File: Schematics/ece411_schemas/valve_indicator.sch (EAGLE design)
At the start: 66 parts, among them IC1 STM32F042K6T6, T1 2N2222, T2 2N2222, T3 2N2222, T4 2N2222, U1 DIODES_INC._AZ34063UMTR-G1DIO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, U2 DIODES_INC._AZ34063UMTR-G1DIO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

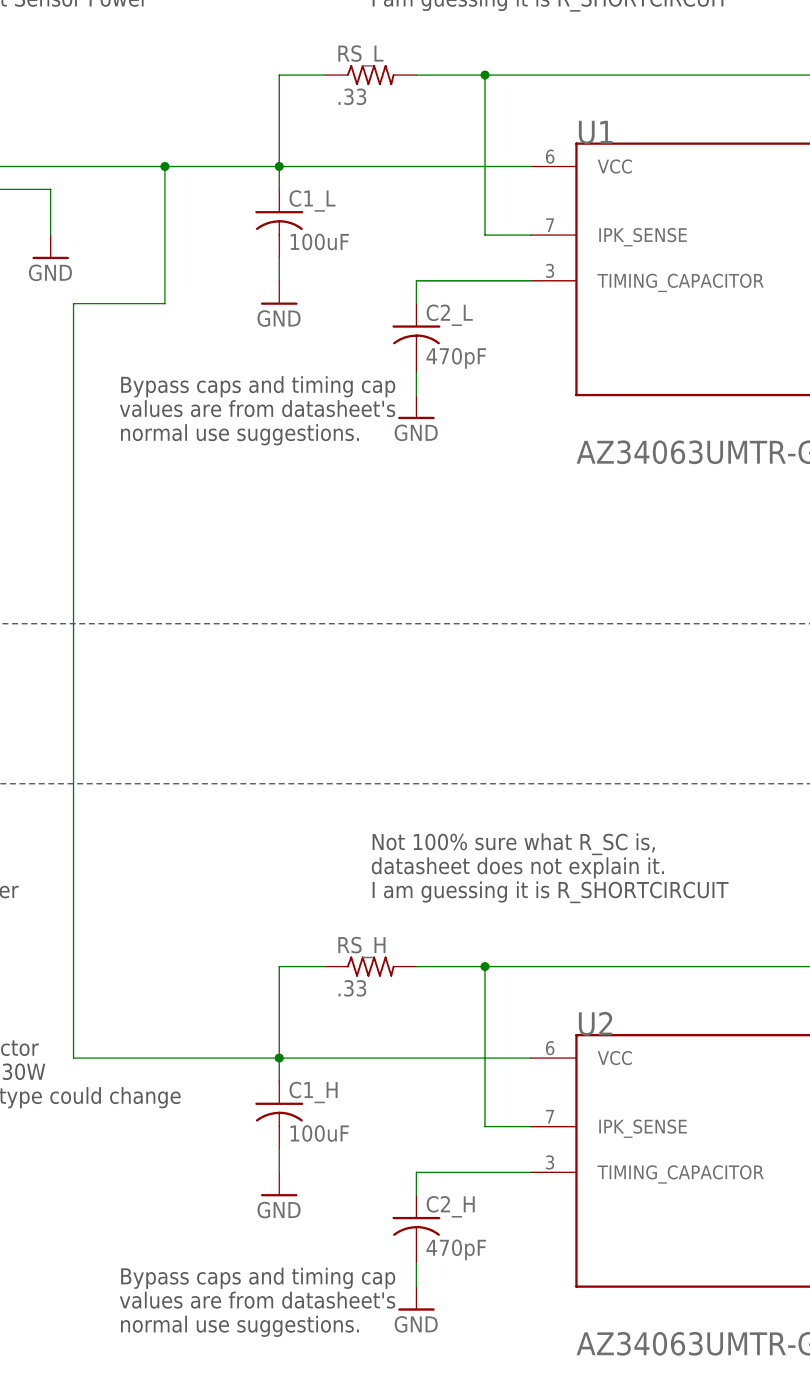
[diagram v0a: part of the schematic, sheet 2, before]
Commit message: added bypass caps, updated bom
needed to add 10uF ceramic in parallel with 100uF electro caps to decrease resistance to ground
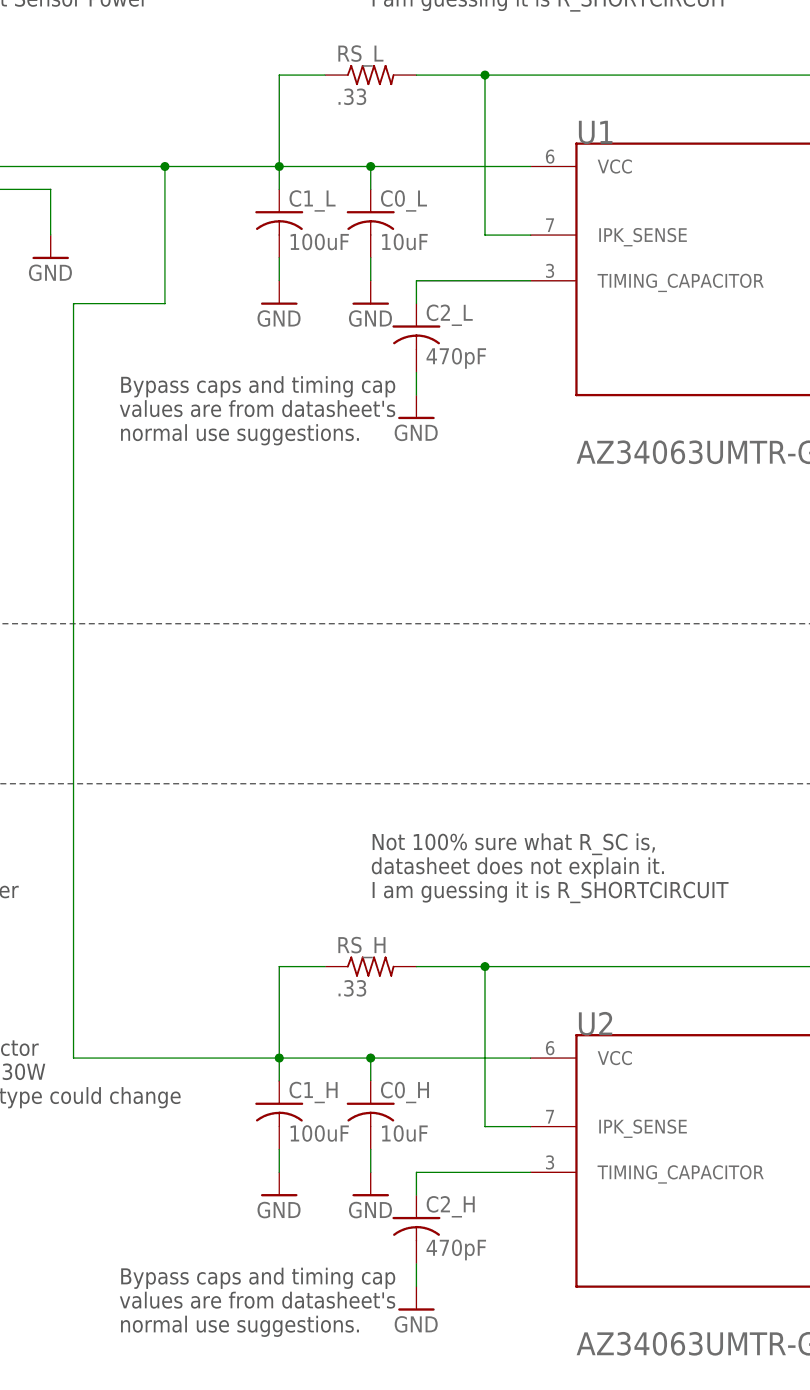
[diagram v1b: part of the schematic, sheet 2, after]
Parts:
- added C0_H, C0_L: 10uF, rcl:C-USC1206
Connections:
- net GND: now also C0_H.2, C0_L.2
- net N$1: now also C0_H.1, C0_L.1
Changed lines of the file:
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@@
 <attribute name="MPN" value="107CKR050M"/>
 </part>
+<part name="C0_L" library="rcl" library_urn="urn:adsk.eagle:library:334" deviceset="C-US" device="C1206" package3d_urn="urn:adsk.eagle:package:23618/2" value="10uF"/>
+<part name="C0_H" library="rcl" library_urn="urn:adsk.eagle:library:334" deviceset="C-US" device="C1206" package3d_urn="urn:adsk.eagle:package:23618/2" value="10uF"/>
+<part name="GND41" library="supply1" library_urn="urn:adsk.eagle:library:371" deviceset="GND" device=""/>
+<part name="GND42" library="supply1" library_urn="urn:adsk.eagle:library:371" deviceset="GND" device=""/>
 </parts>
 <sheets>
@@
 <attribute name="MFR" x="121.92" y="109.22" size="1.778" layer="96" display="off"/>
 </instance>
+<instance part="C0_L" gate="G$1" x="132.08" y="208.28" smashed="yes">
+<attribute name="NAME" x="133.096" y="208.915" size="1.778" layer="95"/>
+<attribute name="VALUE" x="133.096" y="204.089" size="1.778" layer="96"/>
+</instance>
+<instance part="C0_H" gate="G$1" x="132.08" y="109.22" smashed="yes">
+<attribute name="NAME" x="133.096" y="109.855" size="1.778" layer="95"/>
+<attribute name="VALUE" x="133.096" y="105.029" size="1.778" layer="96"/>
+</instance>
+<instance part="GND41" gate="1" x="132.08" y="99.06" smashed="yes">
+<attribute name="VALUE" x="129.54" y="96.52" size="1.778" layer="96"/>
+</instance>
+<instance part="GND42" gate="1" x="132.08" y="198.12" smashed="yes">
+<attribute name="VALUE" x="129.54" y="195.58" size="1.778" layer="96"/>
+</instance>
 </instances>
 <busses>
@@
 <wire x1="233.68" y1="228.6" x2="238.76" y2="228.6" width="0.1524" layer="91"/>
 <pinref part="R2_L" gate="G$1" pin="1"/>
+</segment>
+<segment>
+<pinref part="C0_H" gate="G$1" pin="2"/>
+<wire x1="132.08" y1="104.14" x2="132.08" y2="101.6" width="0.1524" layer="91"/>
+<pinref part="GND41" gate="1" pin="GND"/>
+</segment>
+<segment>
+<pinref part="GND42" gate="1" pin="GND"/>
+<pinref part="C0_L" gate="G$1" pin="2"/>
+<wire x1="132.08" y1="200.66" x2="132.08" y2="203.2" width="0.1524" layer="91"/>
 </segment>
 </net>
@@
 <segment>
 <pinref part="U2" gate="G$0" pin="VCC"/>
-<wire x1="121.92" y1="114.3" x2="149.86" y2="114.3" width="0.1524" layer="91"/>
+<wire x1="121.92" y1="114.3" x2="132.08" y2="114.3" width="0.1524" layer="91"/>
+<wire x1="132.08" y1="114.3" x2="149.86" y2="114.3" width="0.1524" layer="91"/>
 <wire x1="121.92" y1="111.76" x2="121.92" y2="114.3" width="0.1524" layer="91"/>
 <junction x="121.92" y="114.3"/>
@@
 <pinref part="U1" gate="G$0" pin="VCC"/>
 <wire x1="109.22" y1="213.36" x2="121.92" y2="213.36" width="0.1524" layer="91"/>
-<wire x1="121.92" y1="213.36" x2="149.86" y2="213.36" width="0.1524" layer="91"/>
+<wire x1="121.92" y1="213.36" x2="132.08" y2="213.36" width="0.1524" layer="91"/>
+<wire x1="132.08" y1="213.36" x2="149.86" y2="213.36" width="0.1524" layer="91"/>
 <wire x1="121.92" y1="210.82" x2="121.92" y2="213.36" width="0.1524" layer="91"/>
 <junction x="121.92" y="213.36"/>
@@
 <pinref part="C1_L" gate="G$1" pin="1"/>
 <pinref part="C1_H" gate="G$1" pin="1"/>
-</segment>
-</net>
+<pinref part="C0_H" gate="G$1" pin="1"/>
+<wire x1="132.08" y1="111.76" x2="132.08" y2="114.3" width="0.1524" layer="91"/>
+<junction x="132.08" y="114.3"/>
+<pinref part="C0_L" gate="G$1" pin="1"/>
+<wire x1="132.08" y1="210.82" x2="132.08" y2="213.36" width="0.1524" layer="91"/>
+<junction x="132.08" y="213.36"/>
+</segment>
+</net>

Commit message: added bat backup
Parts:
- added BATT_BACKUP: (no value), SparkFun-Connectors:JST_2MM_MALE
- added SB240: (no value), diode:SCHOTTKY-DIODECB417-15
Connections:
- new net N$10: SB240.C
- new net N$16: BATT_BACKUP.+, SB240.A
- net GND: now also BATT_BACKUP.-
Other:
- note added: "Battery Backup System:"
- note added: "Schottky Diode with 2A forward current. Safe to 40V reverse voltage. Forward voltage drop of 0.5v"
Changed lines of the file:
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@@
 <part name="GND41" library="supply1" library_urn="urn:adsk.eagle:library:371" deviceset="GND" device=""/>
 <part name="GND42" library="supply1" library_urn="urn:adsk.eagle:library:371" deviceset="GND" device=""/>
+<part name="BATT_BACKUP" library="SparkFun-Connectors" library_urn="urn:adsk.eagle:library:513" deviceset="JST_2MM_MALE" device="" package3d_urn="urn:adsk.eagle:package:38042/1"/>
+<part name="GND43" library="supply1" library_urn="urn:adsk.eagle:library:371" deviceset="GND" device=""/>
+<part name="SB240" library="diode" library_urn="urn:adsk.eagle:library:210" deviceset="SCHOTTKY-DIODE" device="CB417-15" package3d_urn="urn:adsk.eagle:package:43349/2"/>
 </parts>
 <sheets>
@@
 <text x="297.18" y="119.38" size="1.778" layer="97">10V power all LEDs and Buzzer</text>
 <text x="50.8" y="132.08" size="1.778" layer="97">POE+ Power Supply to 10V LED Power</text>
+<wire x1="340.36" y1="162.56" x2="48.26" y2="162.56" width="0.1524" layer="97" style="shortdash"/>
+<wire x1="48.26" y1="162.56" x2="48.26" y2="243.84" width="0.1524" layer="97" style="shortdash"/>
+<text x="12.7" y="182.88" size="1.778" layer="91">Battery Backup System:</text>
+<text x="33.02" y="165.1" size="1.778" layer="91">Schottky Diode with 2A forward current.
+Safe to 40V reverse voltage. Forward voltage drop of 0.5v</text>
 </plain>
 <instances>
@@
 <attribute name="VALUE" x="129.54" y="195.58" size="1.778" layer="96"/>
 </instance>
+<instance part="BATT_BACKUP" gate="G$1" x="15.24" y="172.72" smashed="yes">
+<attribute name="NAME" x="12.7" y="178.562" size="1.778" layer="95"/>
+</instance>
+<instance part="GND43" gate="1" x="15.24" y="154.94" smashed="yes">
+<attribute name="VALUE" x="12.7" y="152.4" size="1.778" layer="96"/>
+</instance>
+<instance part="SB240" gate="G$1" x="35.56" y="154.94" smashed="yes">
+<attribute name="NAME" x="33.274" y="156.845" size="1.778" layer="95"/>
+<attribute name="VALUE" x="33.274" y="151.511" size="1.778" layer="96"/>
+</instance>
 </instances>
 <busses>
@@
 <pinref part="C0_L" gate="G$1" pin="2"/>
 <wire x1="132.08" y1="200.66" x2="132.08" y2="203.2" width="0.1524" layer="91"/>
+</segment>
+<segment>
+<pinref part="BATT_BACKUP" gate="G$1" pin="-"/>
+<pinref part="GND43" gate="1" pin="GND"/>
+<wire x1="15.24" y1="167.64" x2="15.24" y2="157.48" width="0.1524" layer="91"/>
 </segment>
 </net>
@@
 </segment>
 </net>
+<net name="N$10" class="0">
+<segment>
+<pinref part="SB240" gate="G$1" pin="C"/>
+<wire x1="38.1" y1="154.94" x2="99.06" y2="154.94" width="0.1524" layer="91"/>
+</segment>
+</net>
+<net name="N$16" class="0">
+<segment>
+<pinref part="BATT_BACKUP" gate="G$1" pin="+"/>
+<pinref part="SB240" gate="G$1" pin="A"/>
+<wire x1="17.78" y1="167.64" x2="17.78" y2="154.94" width="0.1524" layer="91"/>
+<wire x1="17.78" y1="154.94" x2="33.02" y2="154.94" width="0.1524" layer="91"/>
+</segment>
+</net>

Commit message: updates to board, added libraries
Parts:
- removed JTAG_EMUL: JTAG_EMUL, pinhead:PINHD-1X5
- removed SB240: (no value), diode:SCHOTTKY-DIODECB417-15
- added D3: SB240, diode:1N5817-B
- added J1: 1.27MM-SWD-CONNECTOR, J-CNC-3220-10-0100-00-ARM-SWD-port:1.27MM-SWD-CONNECTOR
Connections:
- removed net N$10: SB240.C
- net GND: no longer JTAG_EMUL.2
- net N$1: now also D3.C
- net N$16: now also D3.A; no longer SB240.A
- net N$30: now also J1.SWDIO/TMS; no longer JTAG_EMUL.3
- net N$31: now also J1.SWDCLK/TCK; no longer JTAG_EMUL.4
- net N$9: no longer JTAG_EMUL.5
- net VCC: no longer JTAG_EMUL.1
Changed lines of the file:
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@@
 <part name="P+2" library="supply1" library_urn="urn:adsk.eagle:library:371" deviceset="VCC" device="" value="3V6"/>
 <part name="GND25" library="supply1" library_urn="urn:adsk.eagle:library:371" deviceset="GND" device=""/>
-<part name="JTAG_EMUL" library="pinhead" library_urn="urn:adsk.eagle:library:325" deviceset="PINHD-1X5" device="" package3d_urn="urn:adsk.eagle:package:22469/2" value="JTAG_EMUL"/>
 <part name="P+12" library="supply1" library_urn="urn:adsk.eagle:library:371" deviceset="VCC" device="" value="3V6"/>
 <part name="GND26" library="supply1" library_urn="urn:adsk.eagle:library:371" deviceset="GND" device=""/>
@@
 <part name="BATT_BACKUP" library="SparkFun-Connectors" library_urn="urn:adsk.eagle:library:513" deviceset="JST_2MM_MALE" device="" package3d_urn="urn:adsk.eagle:package:38042/1"/>
 <part name="GND43" library="supply1" library_urn="urn:adsk.eagle:library:371" deviceset="GND" device=""/>
-<part name="SB240" library="diode" library_urn="urn:adsk.eagle:library:210" deviceset="SCHOTTKY-DIODE" device="CB417-15" package3d_urn="urn:adsk.eagle:package:43349/2"/>
+<part name="D3" library="diode" library_urn="urn:adsk.eagle:library:210" deviceset="1N581*" device="" package3d_urn="urn:adsk.eagle:package:43421/1" technology="7-B" value="SB240"/>
+<part name="J1" library="J-CNC-3220-10-0100-00-ARM-SWD-port" deviceset="1.27MM-SWD-CONNECTOR" device=""/>
 </parts>
 <sheets>
@@
 <attribute name="VALUE" x="195.58" y="68.58" size="1.778" layer="96"/>
 </instance>
-<instance part="JTAG_EMUL" gate="A" x="137.16" y="215.9" smashed="yes">
-<attribute name="NAME" x="130.81" y="224.155" size="1.778" layer="95"/>
-</instance>
 <instance part="P+12" gate="VCC" x="124.46" y="231.14" smashed="yes">
 <attribute name="VALUE" x="124.46" y="233.68" size="1.778" layer="96" rot="R180"/>
@@
 <attribute name="VALUE" x="347.472" y="40.7162" size="1.778" layer="96"/>
 </instance>
+<instance part="J1" gate="J" x="86.36" y="213.36" smashed="yes">
+<attribute name="NAME" x="80.01" y="231.775" size="1.778" layer="95"/>
+</instance>
 </instances>
 <busses>
@@
 <wire x1="198.12" y1="81.28" x2="198.12" y2="73.66" width="0.1524" layer="91"/>
 <pinref part="GND25" gate="1" pin="GND"/>
-</segment>
-<segment>
-<pinref part="JTAG_EMUL" gate="A" pin="2"/>
-<wire x1="134.62" y1="218.44" x2="124.46" y2="218.44" width="0.1524" layer="91"/>
-<wire x1="124.46" y1="218.44" x2="124.46" y2="208.28" width="0.1524" layer="91"/>
-<pinref part="GND26" gate="1" pin="GND"/>
 </segment>
 <segment>
@@
 </segment>
 <segment>
-<pinref part="JTAG_EMUL" gate="A" pin="1"/>
-<wire x1="134.62" y1="220.98" x2="124.46" y2="220.98" width="0.1524" layer="91"/>
-<wire x1="124.46" y1="220.98" x2="124.46" y2="228.6" width="0.1524" layer="91"/>
-<pinref part="P+12" gate="VCC" pin="VCC"/>
-</segment>
-<segment>
 <pinref part="SD_CARD" gate="A" pin="2"/>
 <wire x1="330.2" y1="106.68" x2="347.98" y2="106.68" width="0.1524" layer="91"/>
@@
 <net name="N$31" class="0">
 <segment>
-<pinref part="JTAG_EMUL" gate="A" pin="4"/>
 <pinref part="IC1" gate="G$1" pin="PA14"/>
-<wire x1="210.82" y1="116.84" x2="218.44" y2="116.84" width="0.1524" layer="91"/>
-<wire x1="218.44" y1="116.84" x2="218.44" y2="213.36" width="0.1524" layer="91"/>
-<wire x1="218.44" y1="213.36" x2="134.62" y2="213.36" width="0.1524" layer="91"/>
+<wire x1="210.82" y1="116.84" x2="215.9" y2="116.84" width="0.1524" layer="91"/>
+<label x="139.7" y="220.98" size="1.778" layer="95"/>
+<pinref part="J1" gate="J" pin="SWDCLK/TCK"/>
+<wire x1="78.74" y1="220.98" x2="215.9" y2="220.98" width="0.1524" layer="91"/>
+<wire x1="215.9" y1="220.98" x2="215.9" y2="116.84" width="0.1524" layer="91"/>
 </segment>
 </net>
@@
 <segment>
 <pinref part="IC1" gate="G$1" pin="PA13"/>
-<wire x1="220.98" y1="215.9" x2="220.98" y2="114.3" width="0.1524" layer="91"/>
-<wire x1="220.98" y1="114.3" x2="210.82" y2="114.3" width="0.1524" layer="91"/>
-<pinref part="JTAG_EMUL" gate="A" pin="3"/>
-<wire x1="220.98" y1="215.9" x2="134.62" y2="215.9" width="0.1524" layer="91"/>
+<label x="139.7" y="226.06" size="1.778" layer="95"/>
+<wire x1="210.82" y1="114.3" x2="210.82" y2="208.28" width="0.1524" layer="91"/>
+<wire x1="210.82" y1="208.28" x2="198.12" y2="208.28" width="0.1524" layer="91"/>
+<pinref part="J1" gate="J" pin="SWDIO/TMS"/>
+<wire x1="78.74" y1="226.06" x2="198.12" y2="226.06" width="0.1524" layer="91"/>
+<wire x1="198.12" y1="226.06" x2="198.12" y2="208.28" width="0.1524" layer="91"/>
 </segment>
 </net>
@@
 <pinref part="IC1" gate="G$1" pin="NRST"/>
 <wire x1="170.18" y1="109.22" x2="157.48" y2="109.22" width="0.1524" layer="91"/>
-<wire x1="157.48" y1="109.22" x2="157.48" y2="210.82" width="0.1524" layer="91"/>
-<pinref part="JTAG_EMUL" gate="A" pin="5"/>
-<wire x1="157.48" y1="210.82" x2="134.62" y2="210.82" width="0.1524" layer="91"/>
+</segment>
+</net>
+<net name="N$10" class="0">
+<segment>
+<wire x1="134.62" y1="220.98" x2="124.46" y2="220.98" width="0.1524" layer="91"/>
 </segment>
 </net>
@@
 <wire x1="48.26" y1="243.84" x2="340.36" y2="243.84" width="0.1524" layer="97" style="shortdash"/>
 <wire x1="340.36" y1="243.84" x2="340.36" y2="162.56" width="0.1524" layer="97" style="shortdash"/>
-<wire x1="340.36" y1="162.56" x2="48.26" y2="162.56" width="0.1524" layer="97" style="shortdash"/>
-<wire x1="48.26" y1="162.56" x2="48.26" y2="243.84" width="0.1524" layer="97" style="shortdash"/>
 <text x="50.8" y="236.22" size="2.54" layer="97">Regulator 1:
 POE+ 24V to 3.6V</text>
@@
 <wire x1="340.36" y1="162.56" x2="48.26" y2="162.56" width="0.1524" layer="97" style="shortdash"/>
 <wire x1="48.26" y1="162.56" x2="48.26" y2="243.84" width="0.1524" layer="97" style="shortdash"/>
-<text x="12.7" y="182.88" size="1.778" layer="91">Battery Backup System:</text>
-<text x="33.02" y="165.1" size="1.778" layer="91">Schottky Diode with 2A forward current.
+<text x="12.7" y="182.88" size="1.778" layer="97">Battery Backup System:</text>
+<text x="33.02" y="165.1" size="1.778" layer="97">Schottky Diode with 2A forward current.
 Safe to 40V reverse voltage. Forward voltage drop of 0.5v</text>
 </plain>
@@
 <attribute name="VALUE" x="12.7" y="152.4" size="1.778" layer="96"/>
 </instance>
-<instance part="SB240" gate="G$1" x="35.56" y="154.94" smashed="yes">
+<instance part="D3" gate="G$1" x="35.56" y="154.94" smashed="yes">
 <attribute name="NAME" x="33.274" y="156.845" size="1.778" layer="95"/>
 <attribute name="VALUE" x="33.274" y="151.511" size="1.778" layer="96"/>
@@
 <wire x1="121.92" y1="124.46" x2="127" y2="124.46" width="0.1524" layer="91"/>
 <wire x1="121.92" y1="114.3" x2="99.06" y2="114.3" width="0.1524" layer="91"/>
-<wire x1="99.06" y1="114.3" x2="99.06" y2="198.12" width="0.1524" layer="91"/>
+<wire x1="99.06" y1="114.3" x2="99.06" y2="154.94" width="0.1524" layer="91"/>
+<wire x1="99.06" y1="154.94" x2="99.06" y2="198.12" width="0.1524" layer="91"/>
 <wire x1="99.06" y1="198.12" x2="109.22" y2="198.12" width="0.1524" layer="91"/>
 <pinref part="U1" gate="G$0" pin="VCC"/>
@@
 <wire x1="132.08" y1="210.82" x2="132.08" y2="213.36" width="0.1524" layer="91"/>
 <junction x="132.08" y="213.36"/>
-</segment>
-</net>
-<net name="N$10" class="0">
-<segment>
-<pinref part="SB240" gate="G$1" pin="C"/>
 <wire x1="38.1" y1="154.94" x2="99.06" y2="154.94" width="0.1524" layer="91"/>
+<pinref part="D3" gate="G$1" pin="C"/>
+<junction x="99.06" y="154.94"/>
 </segment>
 </net>
@@
 <segment>
 <pinref part="BATT_BACKUP" gate="G$1" pin="+"/>
-<pinref part="SB240" gate="G$1" pin="A"/>
 <wire x1="17.78" y1="167.64" x2="17.78" y2="154.94" width="0.1524" layer="91"/>
 <wire x1="17.78" y1="154.94" x2="33.02" y2="154.94" width="0.1524" layer="91"/>
-</segment>
-</net>
+<pinref part="D3" gate="G$1" pin="A"/>
+</segment>
+</net>

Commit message: updated board
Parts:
- removed BATT_BACKUP: (no value), SparkFun-Connectors:JST_2MM_MALE
- removed IC1: STM32F042K6T6, SamacSys_Parts:STM32F042K6T6
- added BATT: LED1, pinhead:PINHD-1X2
- added C10, C11, C12: 100nF, rcl:C-USC0603
- added U3: STM32F042K6, U-ST-STM32F042K-uC:STM32F042K6
- R1_L: value 4.7k -> 3.6k
- R2_L: value 2.5k -> 2.2k
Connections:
- removed net N$23: IC1.PA11, T2.B
- removed net N$39: R13.2, T4.C
- removed net N$40: R12.2, T3.C
- removed net N$41: R11.2, T2.C
- removed net N$42: R10.2, T1.C
- removed net VCC: C3_L.1, HES1.1, HES2.1, HES3.1, HES4.1, HES5.1, HES6.1, HES7.1, HES8.1, HES9.1, IC1.VDD, IC1.VDDA, IC1.VDDIO2, L1.2, R1.1, R1_L.2, R2.1, R3.1, R4.1, R5.1, R6.1, R7.1, R8.1, R9.1, SD_CARD.2
- new net +12V: BUZZER.1, C3_H.1, HES1.1, HES2.1, HES3.1, HES4.1, HES5.1, HES6.1, HES7.1, HES8.1, HES9.1, L2.2, LED1.1, LED2.1, LED3.1, R1.1, R1_H.2, R2.1, R3.1, R4.1, R5.1, R6.1, R7.1, R8.1, R9.1
- new net N$10: LED1.2, T1.C
- new net N$32: J1.!RESET, U3.NRST
- new net N$33: LED3.2, T3.C
- new net N$34: T4.B, U3.PA0
- new net N$35: T2.B, U3.PA11
- net +3V3: now also C10.1, C11.1, C12.1, C3_L.1, J1.VTREF, L1.2, R1_L.2, SD_CARD.2, U3.VDD, U3.VDDA, U3.VDDIO2; no longer C3_H.1, L2.2, R10.1, R11.1, R12.1, R13.1, R1_H.2
- net GND: now also BATT.2, C10.2, C11.2, C12.2, J1.GND, J1.GND@2, J1.GNDDET, R10.2, R11.2, R12.2, R13.2, U3.VSS; no longer BATT_BACKUP.-, BUZZER.2, IC1.VSS_1, IC1.VSS_2, LED1.2, LED2.2, LED3.2
- net N$11: now also U3.PA5; no longer IC1.PA5
- net N$12: now also U3.PA6; no longer IC1.PA6
- net N$13: now also U3.PA7; no longer IC1.PA7
- net N$14: now also U3.PA8; no longer IC1.PA8
- net N$15: now also U3.PA9; no longer IC1.PA9
- net N$16: now also BATT.1; no longer BATT_BACKUP.+
- net N$17: now also U3.PA4; no longer IC1.PA4
- net N$22: now also U3.PA10; no longer IC1.PA10
- net N$24: now also U3.PA12; no longer IC1.PA12
- net N$25: now also LED2.2, T2.C; no longer IC1.PA0, T4.B
- net N$26: now also R10.1; no longer LED1.1
- net N$27: now also R11.1; no longer LED2.1
- net N$28: now also BUZZER.2, T4.C; no longer LED3.1, T3.E
- net N$29: now also R13.1; no longer BUZZER.1
- net N$30: now also U3.PA13-SWDIO; no longer IC1.PA13
- net N$31: now also R12.1, T3.E; no longer IC1.PA14, J1.SWDCLK/TCK
- net N$6: now also U3.PA1; no longer IC1.PA1
- net N$7: now also U3.PA2; no longer IC1.PA2
- net N$8: now also U3.PA3; no longer IC1.PA3
- net N$9: now also J1.SWDCLK/TCK, U3.PA14-SWCLK; no longer IC1.NRST
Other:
- note added: "V_MAIN = 5/4*(R1+R2)/R2. These values give us nominal V_MAIN = 3.3V"
- note removed: "V_MAIN = 5/4*(R1+R2)/R2. These values give us nominal V_MAIN = 3.6V"
- moved on the sheet: BUZZER, H1, H2, H3, H5, J1, LED1, LED2, LED3, R10, R11, R12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
